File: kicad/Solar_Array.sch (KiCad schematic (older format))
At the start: 25 parts, among them IC1 SPV1040, P1 PV_CELL, Q1 Q_NPN_BCE, U1 LTC2990

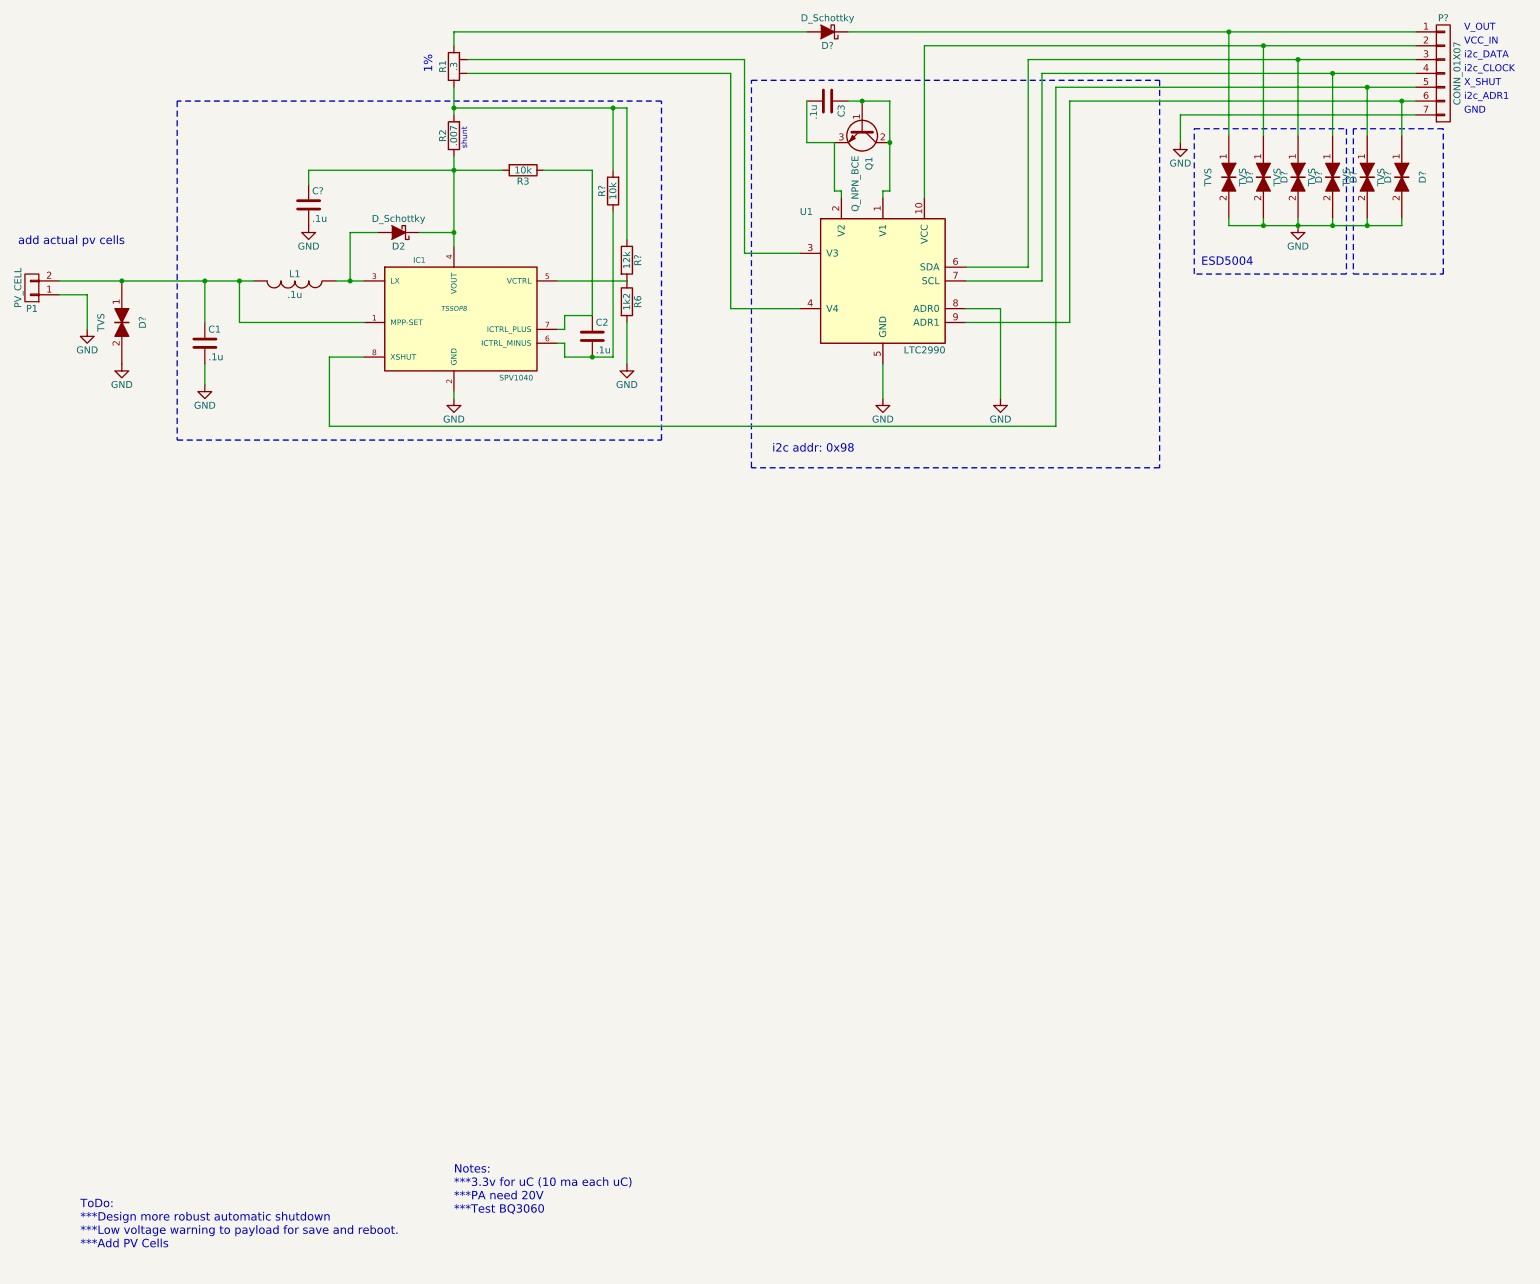
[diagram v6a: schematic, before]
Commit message: Updated todo, updated TVS diode.
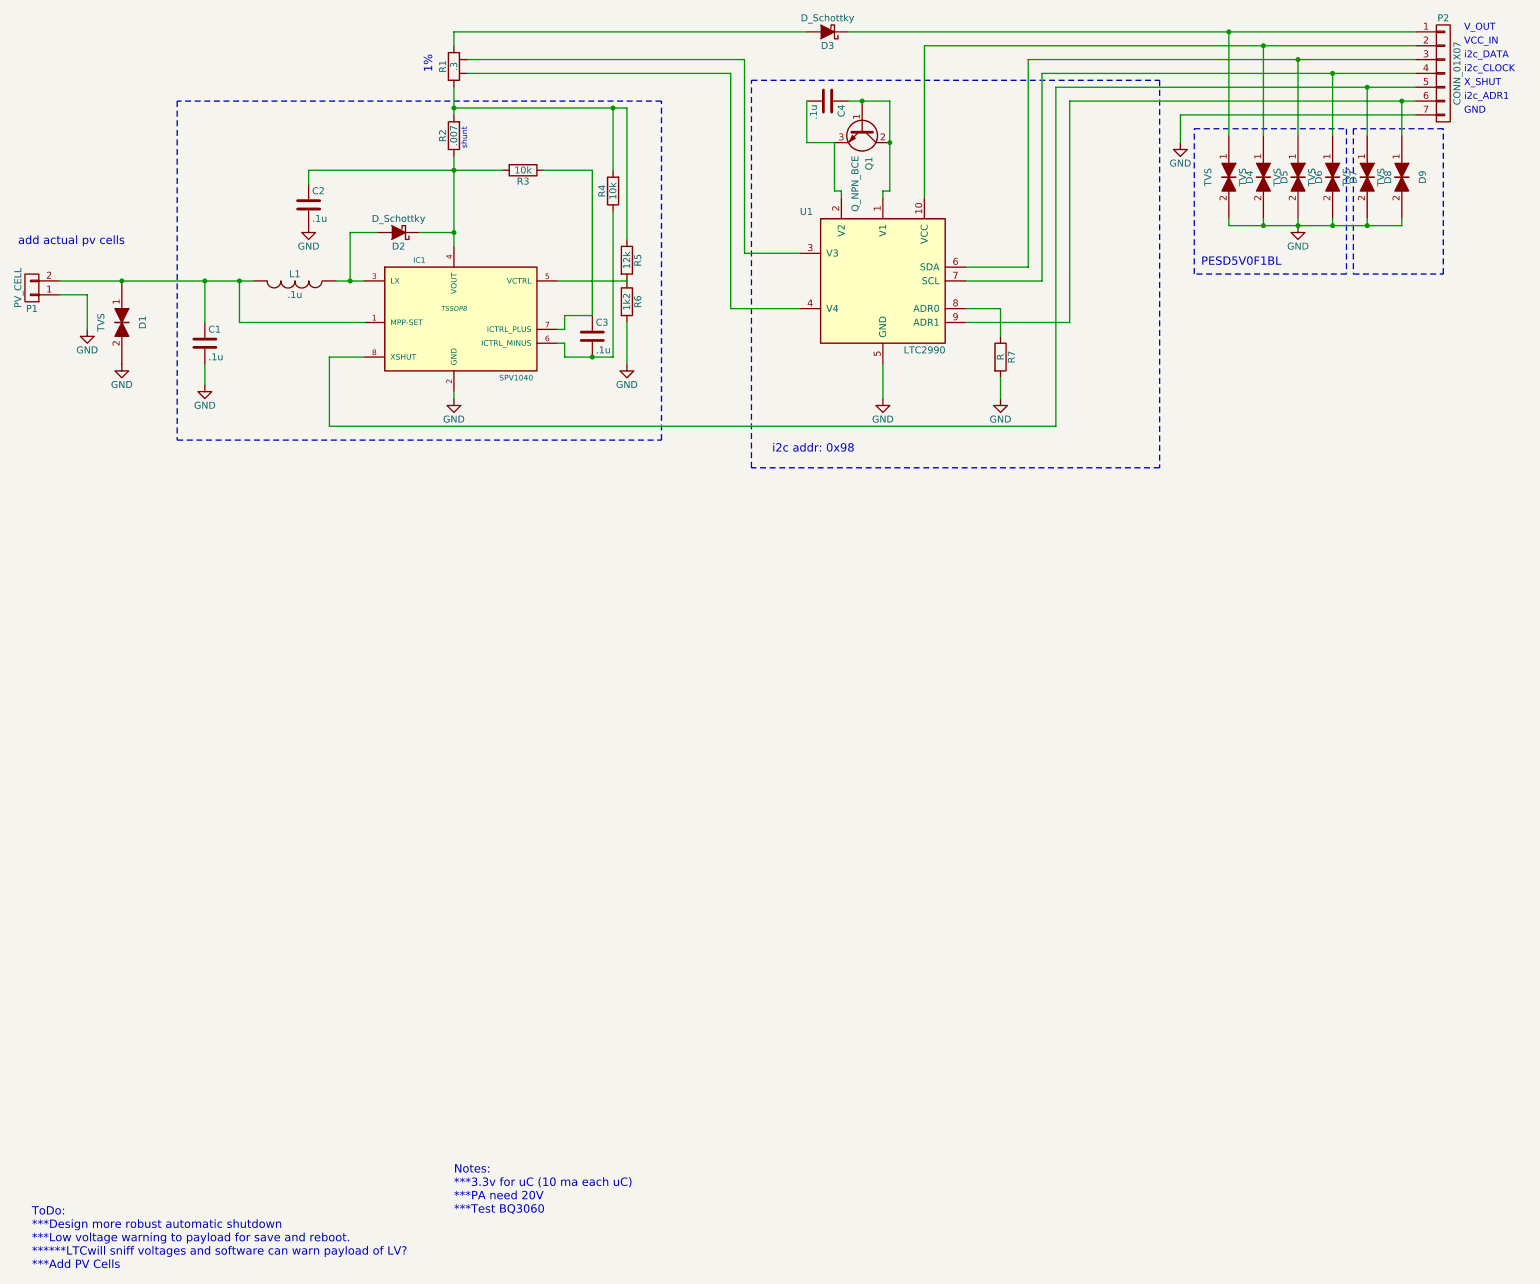
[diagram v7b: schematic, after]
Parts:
- added R7: R, symbol R
- gave numbers to parts that had none: 12
- renumbered C2 to C3, C3 to C4
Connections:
- net GND: now also R7.2; no longer U1.8 (ADR0)
- new net: R7.1, U1.8 (ADR0)
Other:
- note added: "PESD5V0F1BL"
- note added: "ToDo:\n***Design more robust automatic shutdown\n***Low voltage warning to payload for save and reboot.\n******LTCwill sniff voltages and software can warn payload of LV?\n***Add PV Cells"
- note removed: "ESD5004"
- note removed: "ToDo:\n***Design more robust automatic shutdown\n***Low voltage warning to payload for save and reboot.\n***Add PV Cells"
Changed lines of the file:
@@
 $EndComp
 $Comp
-L GND #PWR01
+L GND #PWR7
 U 1 1 56A7969A
 P 7000 3600
-F 0 "#PWR01" H 7000 3350 50  0001 C CNN
+F 0 "#PWR7" H 7000 3350 50  0001 C CNN
 F 1 "GND" H 7000 3450 50  0000 C CNN
 F 2 "" H 7000 3600 60  0000 C CNN
@@
 $EndComp
 $Comp
-L C C3
+L C C4
 U 1 1 56A7975A
 P 6600 1450
-F 0 "C3" H 6625 1550 50  0000 L CNN
+F 0 "C4" H 6625 1550 50  0000 L CNN
 F 1 ".1u" H 6625 1350 50  0000 L CNN
 F 2 "" H 6638 1300 30  0000 C CNN
@@
 	0    1    1    0
 $EndComp
-Text Notes 1200 9750 0    60   ~ 0
-ToDo:\n***Design more robust automatic shutdown\n***Low voltage warning to payload for save and reboot.\n***Add PV Cells
+Text Notes 850  9900 0    60   ~ 0
+ToDo:\n***Design more robust automatic shutdown\n***Low voltage warning to payload for save and reboot.\n******LTCwill sniff voltages and software can warn payload of LV?\n***Add PV Cells
 Text Notes 3750 1250 1    60   ~ 0
 1%
 $Comp
-L GND #PWR02
+L GND #PWR1
 U 1 1 56A96BD7
 P 1250 3100
-F 0 "#PWR02" H 1250 2850 50  0001 C CNN
+F 0 "#PWR1" H 1250 2850 50  0001 C CNN
 F 1 "GND" H 1250 2950 50  0000 C CNN
 F 2 "" H 1250 3100 60  0000 C CNN
@@
 $EndComp
 $Comp
-L GND #PWR03
+L GND #PWR3
 U 1 1 56A97606
 P 2100 3500
-F 0 "#PWR03" H 2100 3250 50  0001 C CNN
+F 0 "#PWR3" H 2100 3250 50  0001 C CNN
 F 1 "GND" H 2100 3350 50  0000 C CNN
 F 2 "" H 2100 3500 60  0000 C CNN
@@
 $EndComp
 $Comp
-L C C2
+L C C3
 U 1 1 56A9778A
 P 4900 3150
-F 0 "C2" H 4925 3250 50  0000 L CNN
+F 0 "C3" H 4925 3250 50  0000 L CNN
 F 1 ".1u" H 4925 3050 50  0000 L CNN
 F 2 "" H 4938 3000 30  0000 C CNN
@@
 $EndComp
 $Comp
-L R R?
+L R R5
 U 1 1 56A97A23
 P 5150 2600
-F 0 "R?" V 5230 2600 50  0000 C CNN
+F 0 "R5" V 5230 2600 50  0000 C CNN
 F 1 "12k" V 5150 2600 50  0000 C CNN
 F 2 "" V 5080 2600 30  0000 C CNN
@@
 $EndComp
 $Comp
-L GND #PWR04
+L GND #PWR6
 U 1 1 56A97B91
 P 5150 3350
-F 0 "#PWR04" H 5150 3100 50  0001 C CNN
+F 0 "#PWR6" H 5150 3100 50  0001 C CNN
 F 1 "GND" H 5150 3200 50  0000 C CNN
 F 2 "" H 5150 3350 60  0000 C CNN
@@
 $EndComp
 $Comp
-L GND #PWR05
+L GND #PWR5
 U 1 1 56A99359
 P 3900 3600
-F 0 "#PWR05" H 3900 3350 50  0001 C CNN
+F 0 "#PWR5" H 3900 3350 50  0001 C CNN
 F 1 "GND" H 3900 3450 50  0000 C CNN
 F 2 "" H 3900 3600 60  0000 C CNN
@@
 $EndComp
 $Comp
-L GND #PWR06
+L GND #PWR9
 U 1 1 56A9DF6A
 P 9150 1750
-F 0 "#PWR06" H 9150 1500 50  0001 C CNN
+F 0 "#PWR9" H 9150 1500 50  0001 C CNN
 F 1 "GND" H 9150 1600 50  0000 C CNN
 F 2 "" H 9150 1750 60  0000 C CNN
@@
 GND
 $Comp
-L D_Schottky D?
+L D_Schottky D3
 U 1 1 56BAC557
 P 6600 950
-F 0 "D?" H 6600 1050 50  0000 C CNN
+F 0 "D3" H 6600 1050 50  0000 C CNN
 F 1 "D_Schottky" H 6600 850 50  0000 C CNN
 F 2 "" H 6600 950 60  0000 C CNN
@@
 $EndComp
 $Comp
-L GND #PWR?
+L GND #PWR8
 U 1 1 56BAE8DD
 P 7850 3600
-F 0 "#PWR?" H 7850 3350 50  0001 C CNN
+F 0 "#PWR8" H 7850 3350 50  0001 C CNN
 F 1 "GND" H 7850 3450 50  0000 C CNN
 F 2 "" H 7850 3600 50  0000 C CNN
@@
 $EndComp
 $Comp
-L CONN_01X07 P?
+L CONN_01X07 P2
 U 1 1 56BAEA85
 P 11050 1250
-F 0 "P?" H 11050 1650 50  0000 C CNN
+F 0 "P2" H 11050 1650 50  0000 C CNN
 F 1 "CONN_01X07" V 11150 1250 50  0000 C CNN
 F 2 "" H 11050 1250 50  0000 C CNN
@@
 i2c_ADR1
 $Comp
-L TVS D?
+L TVS D1
 U 1 1 56BB9867
 P 1500 3050
-F 0 "D?" H 1500 3200 50  0000 C CNN
+F 0 "D1" H 1500 3200 50  0000 C CNN
 F 1 "TVS" H 1500 2900 50  0000 C CNN
 F 2 "" H 1500 3050 50  0000 C CNN
@@
 $EndComp
 $Comp
-L GND #PWR?
+L GND #PWR2
 U 1 1 56BB9B10
 P 1500 3350
-F 0 "#PWR?" H 1500 3100 50  0001 C CNN
+F 0 "#PWR2" H 1500 3100 50  0001 C CNN
 F 1 "GND" H 1500 3200 50  0000 C CNN
 F 2 "" H 1500 3350 50  0000 C CNN
@@
 add actual pv cells
 $Comp
-L TVS D?
+L TVS D4
 U 1 1 56BBB34D
 P 9500 2000
-F 0 "D?" H 9500 2150 50  0000 C CNN
+F 0 "D4" H 9500 2150 50  0000 C CNN
 F 1 "TVS" H 9500 1850 50  0000 C CNN
 F 2 "" H 9500 2000 50  0000 C CNN
@@
 $EndComp
 $Comp
-L TVS D?
+L TVS D5
 U 1 1 56BBB616
 P 9750 2000
-F 0 "D?" H 9750 2150 50  0000 C CNN
+F 0 "D5" H 9750 2150 50  0000 C CNN
 F 1 "TVS" H 9750 1850 50  0000 C CNN
 F 2 "" H 9750 2000 50  0000 C CNN
@@
 $EndComp
 $Comp
-L TVS D?
+L TVS D6
 U 1 1 56BBB6B0
 P 10000 2000
-F 0 "D?" H 10000 2150 50  0000 C CNN
+F 0 "D6" H 10000 2150 50  0000 C CNN
 F 1 "TVS" H 10000 1850 50  0000 C CNN
 F 2 "" H 10000 2000 50  0000 C CNN
@@
 $EndComp
 $Comp
-L TVS D?
+L TVS D7
 U 1 1 56BBB711
 P 10250 2000
-F 0 "D?" H 10250 2150 50  0000 C CNN
+F 0 "D7" H 10250 2150 50  0000 C CNN
 F 1 "TVS" H 10250 1850 50  0000 C CNN
 F 2 "" H 10250 2000 50  0000 C CNN
@@
 $EndComp
 $Comp
-L TVS D?
+L TVS D8
 U 1 1 56BBB769
 P 10500 2000
-F 0 "D?" H 10500 2150 50  0000 C CNN
+F 0 "D8" H 10500 2150 50  0000 C CNN
 F 1 "TVS" H 10500 1850 50  0000 C CNN
 F 2 "" H 10500 2000 50  0000 C CNN
@@
 $EndComp
 $Comp
-L TVS D?
+L TVS D9
 U 1 1 56BBBE2D
 P 10750 2000
-F 0 "D?" H 10750 2150 50  0000 C CNN
+F 0 "D9" H 10750 2150 50  0000 C CNN
 F 1 "TVS" H 10750 1850 50  0000 C CNN
 F 2 "" H 10750 2000 50  0000 C CNN
@@
 	6750 950  10850 950
 Wire Wire Line
-	7850 2950 7850 3600
-Wire Wire Line
 	8350 3050 8350 1450
 Wire Wire Line
@@
 Connection ~ 10500 2350
 $Comp
-L GND #PWR?
+L GND #PWR10
 U 1 1 56BBC663
 P 10000 2350
-F 0 "#PWR?" H 10000 2100 50  0001 C CNN
+F 0 "#PWR10" H 10000 2100 50  0001 C CNN
 F 1 "GND" H 10000 2200 50  0000 C CNN
 F 2 "" H 10000 2350 50  0000 C CNN
@@
 	11050 1650 10400 1650
 Text Notes 9300 2650 0    60   ~ 0
-ESD5004
+PESD5V0F1BL
 Wire Wire Line
 	4900 3000 4900 1950
 $Comp
-L R R?
+L R R4
 U 1 1 56BBD407
 P 5050 2100
-F 0 "R?" V 5130 2100 50  0000 C CNN
+F 0 "R4" V 5130 2100 50  0000 C CNN
 F 1 "10k" V 5050 2100 50  0000 C CNN
 F 2 "" V 4980 2100 30  0000 C CNN
@@
 shunt
 $Comp
-L GND #PWR?
+L GND #PWR4
 U 1 1 56BBD7C0
 P 2850 2350
-F 0 "#PWR?" H 2850 2100 50  0001 C CNN
+F 0 "#PWR4" H 2850 2100 50  0001 C CNN
 F 1 "GND" H 2850 2200 50  0000 C CNN
 F 2 "" H 2850 2350 50  0000 C CNN
@@
 	4900 1950 4550 1950
 $Comp
-L C C?
+L C C2
 U 1 1 56BBDDFD
 P 2850 2200
-F 0 "C?" H 2875 2300 50  0000 L CNN
+F 0 "C2" H 2875 2300 50  0000 L CNN
 F 1 ".1u" H 2875 2100 50  0000 L CNN
 F 2 "" H 2888 2050 50  0000 C CNN
@@
 Wire Wire Line
 	2850 1950 2850 2050
+$Comp
+L R R7
+U 1 1 56BCEAEC
+P 7850 3300
+F 0 "R7" V 7930 3300 50  0000 C CNN
+F 1 "R" V 7850 3300 50  0000 C CNN
+F 2 "" V 7780 3300 50  0000 C CNN
+F 3 "" H 7850 3300 50  0000 C CNN
+	1    7850 3300
+	1    0    0    -1
+$EndComp
+Wire Wire Line
+	7850 3450 7850 3600
+Wire Wire Line
+	7850 2950 7850 3150
 $EndSCHEMATC
